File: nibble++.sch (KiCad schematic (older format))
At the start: 19 parts, among them SW1 SW_DPDT_x2, U1 NE555, U2 4017

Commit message: Renamed project to nibble++
Signed-off-by: Thomas Schmid <tom@binary-kitchen.de>
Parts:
- D1: footprint SMD-Challange:LED_0805_2012Metric_Pad1.15x1.40mm_HandSolder_simple_drawing -> nibble++:LED_0805_2012Metric_Pad1.15x1.40mm_HandSolder_simple_drawing
- D2: footprint SMD-Challange:LED_0603_1608Metric_Pad1.05x0.95mm_HandSolder_simple_drawing -> nibble++:LED_0603_1608Metric_Pad1.05x0.95mm_HandSolder_simple_drawing
- D4, D5: footprint SMD-Challange:LED_0201_0603Metric_hand_soldering -> nibble++:LED_0201_0603Metric_hand_soldering
- R1: footprint Resistor_SMD:R_0805_2012Metric_Pad1.15x1.40mm_HandSolder -> nibble++:R_0805_2012Metric_Pad1.15x1.40mm_HandSolder
- R2: footprint Resistor_SMD:R_0603_1608Metric_Pad1.05x0.95mm_HandSolder -> nibble++:R_0603_1608Metric_Pad1.05x0.95mm_HandSolder
- R4: footprint SMD-Challange:R_0201_0603Metric_hand_soldering -> nibble++:R_0201_0603Metric_hand_soldering
- R5: footprint SMD-Challange:R_01005_0402Metric_hand_soldering -> nibble++:R_01005_0402Metric_hand_soldering
- SW1: footprint SMD-Challange:smd_switch_slide -> nibble++:smd_switch_slide
- U2: footprint SMD-Challange:SOP-16_4.4x10.4mm_P1.27mm_simple_drawing -> nibble++:SOP-16_4.4x10.4mm_P1.27mm_simple_drawing
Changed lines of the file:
@@
 EESchema Schematic File Version 4
-LIBS:SMD-Challange-cache
+LIBS:nibble++-cache
 EELAYER 26 0
 EELAYER END
@@
 F 0 "D1" H 7500 2150 50  0000 C CNN
 F 1 "LED" H 7500 2350 50  0000 C CNN
-F 2 "SMD-Challange:LED_0805_2012Metric_Pad1.15x1.40mm_HandSolder_simple_drawing" H 7500 2250 50  0001 C CNN
+F 2 "nibble++:LED_0805_2012Metric_Pad1.15x1.40mm_HandSolder_simple_drawing" H 7500 2250 50  0001 C CNN
 F 3 "~" H 7500 2250 50  0001 C CNN
 	1    7500 2250
@@
 F 0 "D2" H 7500 2450 50  0000 C CNN
 F 1 "LED" H 7500 2650 50  0000 C CNN
-F 2 "SMD-Challange:LED_0603_1608Metric_Pad1.05x0.95mm_HandSolder_simple_drawing" H 7500 2550 50  0001 C CNN
+F 2 "nibble++:LED_0603_1608Metric_Pad1.05x0.95mm_HandSolder_simple_drawing" H 7500 2550 50  0001 C CNN
 F 3 "~" H 7500 2550 50  0001 C CNN
 	1    7500 2550
@@
 F 0 "D4" H 7500 3050 50  0000 C CNN
 F 1 "LED" H 7500 3250 50  0000 C CNN
-F 2 "SMD-Challange:LED_0201_0603Metric_hand_soldering" H 7500 3150 50  0001 C CNN
+F 2 "nibble++:LED_0201_0603Metric_hand_soldering" H 7500 3150 50  0001 C CNN
 F 3 "~" H 7500 3150 50  0001 C CNN
 	1    7500 3150
@@
 F 0 "D5" H 7500 3350 50  0000 C CNN
 F 1 "LED" H 7500 3550 50  0000 C CNN
-F 2 "SMD-Challange:LED_0201_0603Metric_hand_soldering" H 7500 3450 50  0001 C CNN
+F 2 "nibble++:LED_0201_0603Metric_hand_soldering" H 7500 3450 50  0001 C CNN
 F 3 "~" H 7500 3450 50  0001 C CNN
 	1    7500 3450
@@
 F 0 "R1" V 6993 2250 50  0000 C CNN
 F 1 "100" V 7084 2250 50  0000 C CNN
-F 2 "Resistor_SMD:R_0805_2012Metric_Pad1.15x1.40mm_HandSolder" V 7130 2250 50  0001 C CNN
+F 2 "nibble++:R_0805_2012Metric_Pad1.15x1.40mm_HandSolder" V 7130 2250 50  0001 C CNN
 F 3 "~" H 7200 2250 50  0001 C CNN
 	1    7200 2250
@@
 F 0 "R2" V 6993 2550 50  0000 C CNN
 F 1 "100" V 7084 2550 50  0000 C CNN
-F 2 "Resistor_SMD:R_0603_1608Metric_Pad1.05x0.95mm_HandSolder" V 7130 2550 50  0001 C CNN
+F 2 "nibble++:R_0603_1608Metric_Pad1.05x0.95mm_HandSolder" V 7130 2550 50  0001 C CNN
 F 3 "~" H 7200 2550 50  0001 C CNN
 	1    7200 2550
@@
 F 0 "R4" V 6993 3150 50  0000 C CNN
 F 1 "150" V 7084 3150 50  0000 C CNN
-F 2 "SMD-Challange:R_0201_0603Metric_hand_soldering" V 7130 3150 50  0001 C CNN
+F 2 "nibble++:R_0201_0603Metric_hand_soldering" V 7130 3150 50  0001 C CNN
 F 3 "~" H 7200 3150 50  0001 C CNN
 	1    7200 3150
@@
 F 0 "R5" V 6993 3450 50  0000 C CNN
 F 1 "200" V 7084 3450 50  0000 C CNN
-F 2 "SMD-Challange:R_01005_0402Metric_hand_soldering" V 7130 3450 50  0001 C CNN
+F 2 "nibble++:R_01005_0402Metric_hand_soldering" V 7130 3450 50  0001 C CNN
 F 3 "~" H 7200 3450 50  0001 C CNN
 	1    7200 3450
@@
 F 0 "U2" H 5600 3500 50  0000 C CNN
 F 1 "4017" H 5650 3400 50  0000 C CNN
-F 2 "SMD-Challange:SOP-16_4.4x10.4mm_P1.27mm_simple_drawing" H 5850 2750 50  0001 C CNN
+F 2 "nibble++:SOP-16_4.4x10.4mm_P1.27mm_simple_drawing" H 5850 2750 50  0001 C CNN
 F 3 "http://www.intersil.com/content/dam/Intersil/documents/cd40/cd4017bms-22bms.pdf" H 5850 2750 50  0001 C CNN
 	1    5850 2750
@@
 F 0 "SW1" V 3404 1248 50  0000 L CNN
 F 1 "SW_DPDT_x2" V 3495 1248 50  0000 L CNN
-F 2 "SMD-Challange:smd_switch_slide" H 3450 1100 50  0001 C CNN
+F 2 "nibble++:smd_switch_slide" H 3450 1100 50  0001 C CNN
 F 3 "" H 3450 1100 50  0001 C CNN
 	1    3450 1100

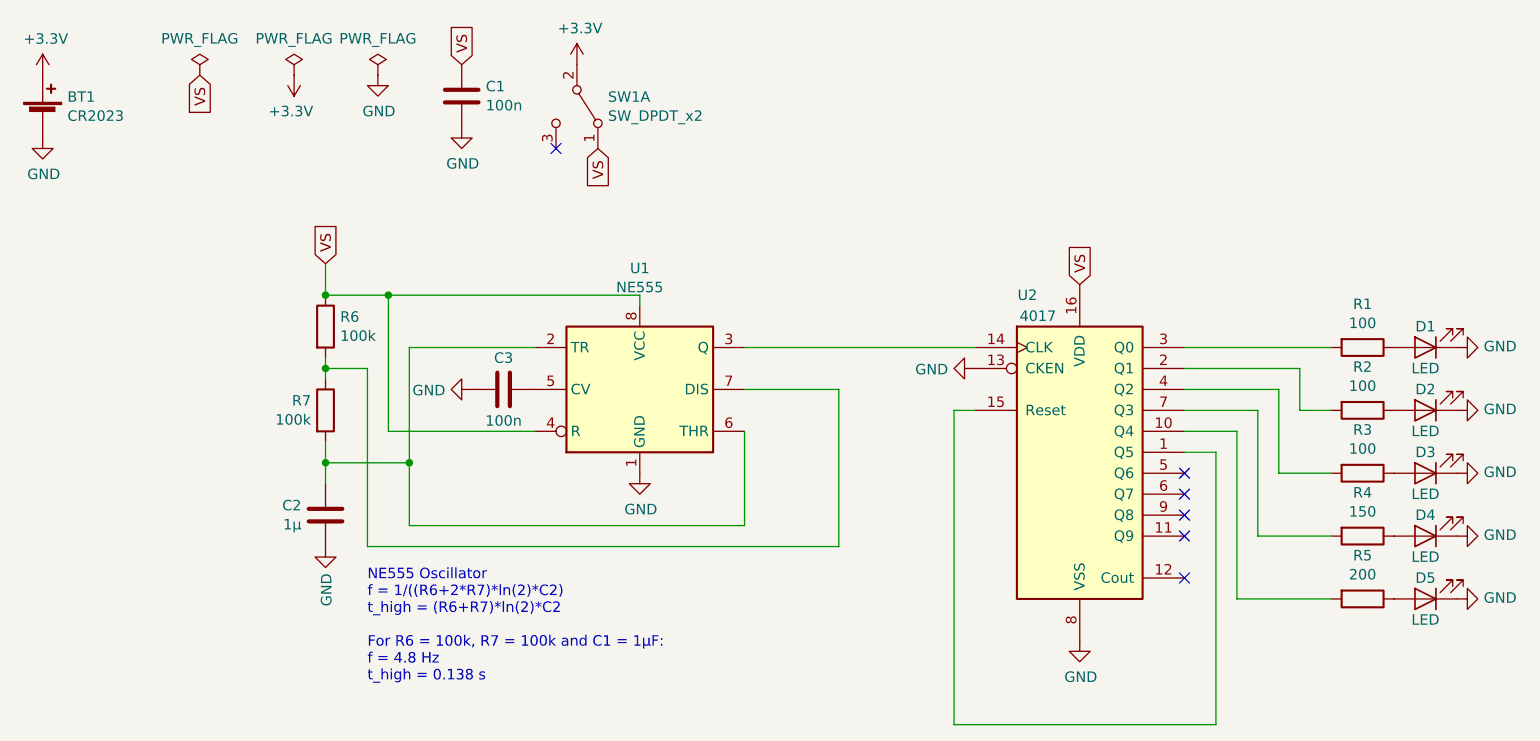
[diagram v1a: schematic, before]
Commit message: added additional information for some parts
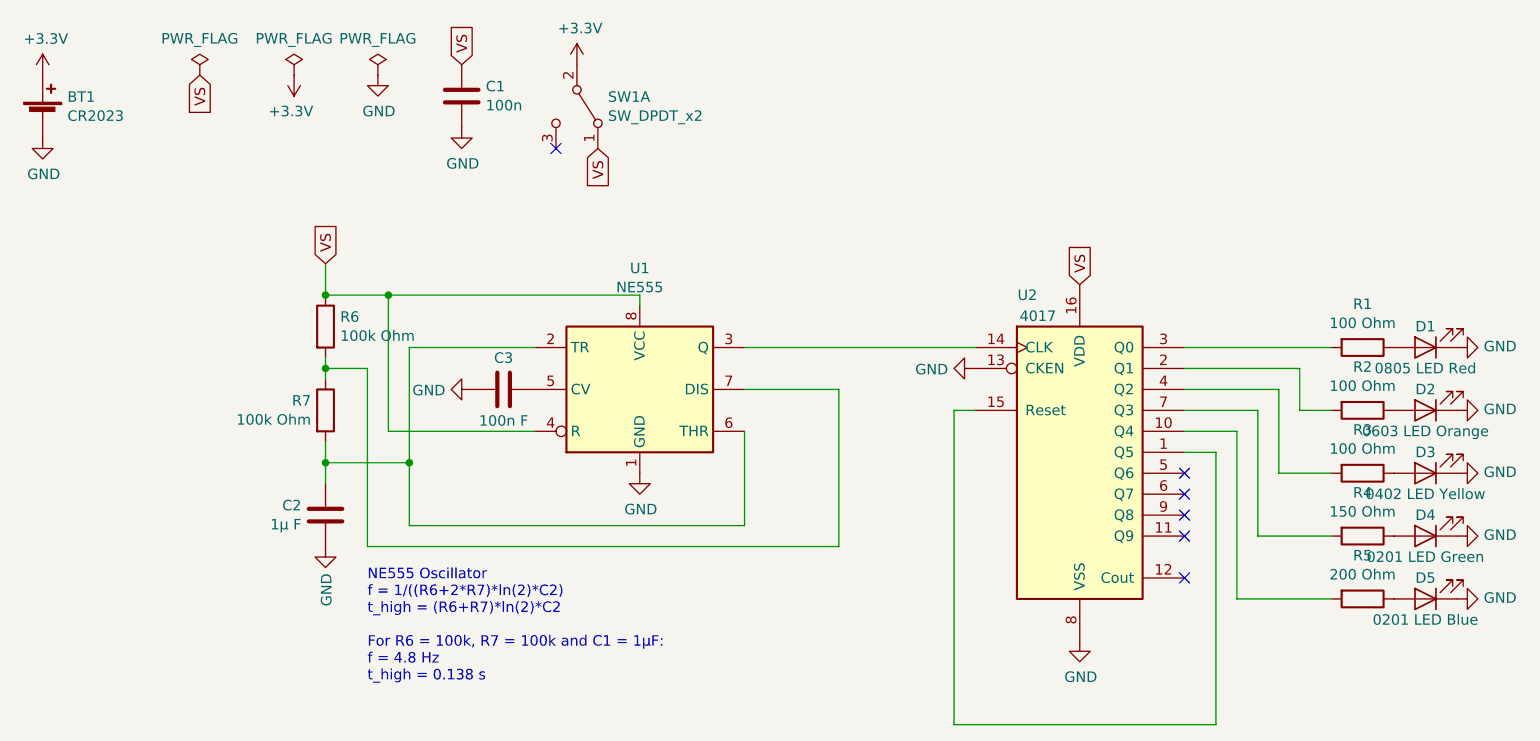
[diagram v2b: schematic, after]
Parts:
- C2: value 1µ -> 1µ F
- C3: value 100n -> 100n F
- D1: value LED -> 0805 LED Red
- D2: value LED -> 0603 LED Orange
- D3: value LED -> 0402 LED Yellow
- D4: value LED -> 0201 LED Green
- D5: value LED -> 0201 LED Blue
- R1, R2, R3: value 100 -> 100 Ohm
- R4: value 150 -> 150 Ohm
- R5: value 200 -> 200 Ohm
- R6, R7: value 100k -> 100k Ohm
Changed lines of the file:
@@
 P 7500 2250
 F 0 "D1" H 7500 2150 50  0000 C CNN
-F 1 "LED" H 7500 2350 50  0000 C CNN
+F 1 "0805 LED Red" H 7500 2350 50  0000 C CNN
 F 2 "nibble++:LED_0805_2012Metric_Pad1.15x1.40mm_HandSolder_simple_drawing" H 7500 2250 50  0001 C CNN
 F 3 "~" H 7500 2250 50  0001 C CNN
@@
 P 7500 2550
 F 0 "D2" H 7500 2450 50  0000 C CNN
-F 1 "LED" H 7500 2650 50  0000 C CNN
+F 1 "0603 LED Orange" H 7500 2650 50  0000 C CNN
 F 2 "nibble++:LED_0603_1608Metric_Pad1.05x0.95mm_HandSolder_simple_drawing" H 7500 2550 50  0001 C CNN
 F 3 "~" H 7500 2550 50  0001 C CNN
@@
 P 7500 2850
 F 0 "D3" H 7500 2750 50  0000 C CNN
-F 1 "LED" H 7500 2950 50  0000 C CNN
+F 1 "0402 LED Yellow" H 7500 2950 50  0000 C CNN
 F 2 "LED_SMD:LED_0402_1005Metric" H 7500 2850 50  0001 C CNN
 F 3 "~" H 7500 2850 50  0001 C CNN
@@
 P 7500 3150
 F 0 "D4" H 7500 3050 50  0000 C CNN
-F 1 "LED" H 7500 3250 50  0000 C CNN
+F 1 "0201 LED Green" H 7500 3250 50  0000 C CNN
 F 2 "nibble++:LED_0201_0603Metric_hand_soldering" H 7500 3150 50  0001 C CNN
 F 3 "~" H 7500 3150 50  0001 C CNN
@@
 P 7500 3450
 F 0 "D5" H 7500 3350 50  0000 C CNN
-F 1 "LED" H 7500 3550 50  0000 C CNN
+F 1 "0201 LED Blue" H 7500 3550 50  0000 C CNN
 F 2 "nibble++:LED_0201_0603Metric_hand_soldering" H 7500 3450 50  0001 C CNN
 F 3 "~" H 7500 3450 50  0001 C CNN
@@
 P 7200 2250
 F 0 "R1" V 6993 2250 50  0000 C CNN
-F 1 "100" V 7084 2250 50  0000 C CNN
+F 1 "100 Ohm" V 7084 2250 50  0000 C CNN
 F 2 "nibble++:R_0805_2012Metric_Pad1.15x1.40mm_HandSolder" V 7130 2250 50  0001 C CNN
 F 3 "~" H 7200 2250 50  0001 C CNN
@@
 P 7200 2550
 F 0 "R2" V 6993 2550 50  0000 C CNN
-F 1 "100" V 7084 2550 50  0000 C CNN
+F 1 "100 Ohm" V 7084 2550 50  0000 C CNN
 F 2 "nibble++:R_0603_1608Metric_Pad1.05x0.95mm_HandSolder" V 7130 2550 50  0001 C CNN
 F 3 "~" H 7200 2550 50  0001 C CNN
@@
 P 7200 2850
 F 0 "R3" V 6993 2850 50  0000 C CNN
-F 1 "100" V 7084 2850 50  0000 C CNN
+F 1 "100 Ohm" V 7084 2850 50  0000 C CNN
 F 2 "Resistor_SMD:R_0402_1005Metric" V 7130 2850 50  0001 C CNN
 F 3 "~" H 7200 2850 50  0001 C CNN
@@
 P 7200 3150
 F 0 "R4" V 6993 3150 50  0000 C CNN
-F 1 "150" V 7084 3150 50  0000 C CNN
+F 1 "150 Ohm" V 7084 3150 50  0000 C CNN
 F 2 "nibble++:R_0201_0603Metric_hand_soldering" V 7130 3150 50  0001 C CNN
 F 3 "~" H 7200 3150 50  0001 C CNN
@@
 P 7200 3450
 F 0 "R5" V 6993 3450 50  0000 C CNN
-F 1 "200" V 7084 3450 50  0000 C CNN
+F 1 "200 Ohm" V 7084 3450 50  0000 C CNN
 F 2 "nibble++:R_01005_0402Metric_hand_soldering" V 7130 3450 50  0001 C CNN
 F 3 "~" H 7200 3450 50  0001 C CNN
@@
 P 3100 2450
 F 0 "C3" V 2950 2450 50  0000 C CNN
-F 1 "100n" V 3250 2450 50  0000 C CNN
+F 1 "100n F" V 3250 2450 50  0000 C CNN
 F 2 "Capacitor_SMD:C_0805_2012Metric_Pad1.15x1.40mm_HandSolder" H 3138 2300 50  0001 C CNN
 F 3 "~" H 3100 2450 50  0001 C CNN
@@
 P 2250 2150
 F 0 "R6" H 2320 2196 50  0000 L CNN
-F 1 "100k" H 2320 2105 50  0000 L CNN
+F 1 "100k Ohm" H 2320 2105 50  0000 L CNN
 F 2 "Resistor_SMD:R_0805_2012Metric_Pad1.15x1.40mm_HandSolder" V 2180 2150 50  0001 C CNN
 F 3 "~" H 2250 2150 50  0001 C CNN
@@
 P 2250 2550
 F 0 "R7" H 2181 2596 50  0000 R CNN
-F 1 "100k" H 2181 2505 50  0000 R CNN
+F 1 "100k Ohm" H 2181 2505 50  0000 R CNN
 F 2 "Resistor_SMD:R_0805_2012Metric_Pad1.15x1.40mm_HandSolder" V 2180 2550 50  0001 C CNN
 F 3 "~" H 2250 2550 50  0001 C CNN
@@
 P 2250 3050
 F 0 "C2" H 2365 3004 50  0000 L CNN
-F 1 "1µ" H 2365 3095 50  0000 L CNN
+F 1 "1µ F" H 2365 3095 50  0000 L CNN
 F 2 "Capacitor_SMD:C_0805_2012Metric_Pad1.15x1.40mm_HandSolder" H 2288 2900 50  0001 C CNN
 F 3 "~" H 2250 3050 50  0001 C CNN

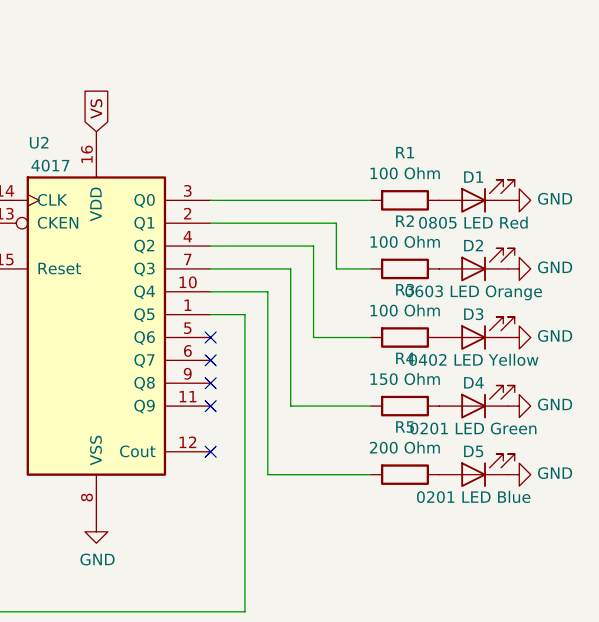
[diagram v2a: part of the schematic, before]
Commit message: modified resistor value. fixing #3
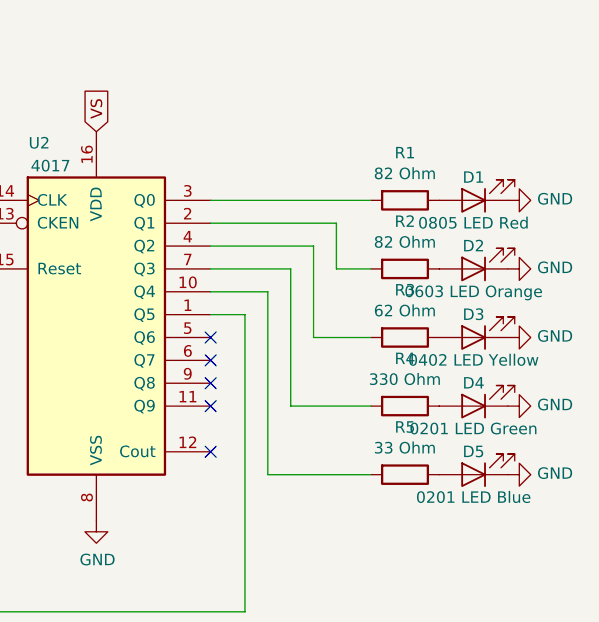
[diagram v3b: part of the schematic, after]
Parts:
- R1, R2: value 100 Ohm -> 82 Ohm
- R3: value 100 Ohm -> 62 Ohm
- R4: value 150 Ohm -> 330 Ohm
- R5: value 200 Ohm -> 33 Ohm
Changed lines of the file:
@@
 EESchema Schematic File Version 4
 LIBS:nibble++-cache
-EELAYER 26 0
+EELAYER 29 0
 EELAYER END
 $Descr A4 11693 8268
@@
 P 7200 2250
 F 0 "R1" V 6993 2250 50  0000 C CNN
-F 1 "100 Ohm" V 7084 2250 50  0000 C CNN
+F 1 "82 Ohm" V 7084 2250 50  0000 C CNN
 F 2 "nibble++:R_0805_2012Metric_Pad1.15x1.40mm_HandSolder" V 7130 2250 50  0001 C CNN
 F 3 "~" H 7200 2250 50  0001 C CNN
@@
 P 7200 2550
 F 0 "R2" V 6993 2550 50  0000 C CNN
-F 1 "100 Ohm" V 7084 2550 50  0000 C CNN
+F 1 "82 Ohm" V 7084 2550 50  0000 C CNN
 F 2 "nibble++:R_0603_1608Metric_Pad1.05x0.95mm_HandSolder" V 7130 2550 50  0001 C CNN
 F 3 "~" H 7200 2550 50  0001 C CNN
@@
 P 7200 2850
 F 0 "R3" V 6993 2850 50  0000 C CNN
-F 1 "100 Ohm" V 7084 2850 50  0000 C CNN
+F 1 "62 Ohm" V 7084 2850 50  0000 C CNN
 F 2 "Resistor_SMD:R_0402_1005Metric" V 7130 2850 50  0001 C CNN
 F 3 "~" H 7200 2850 50  0001 C CNN
@@
 P 7200 3150
 F 0 "R4" V 6993 3150 50  0000 C CNN
-F 1 "150 Ohm" V 7084 3150 50  0000 C CNN
+F 1 "330 Ohm" V 7084 3150 50  0000 C CNN
 F 2 "nibble++:R_0201_0603Metric_hand_soldering" V 7130 3150 50  0001 C CNN
 F 3 "~" H 7200 3150 50  0001 C CNN
@@
 P 7200 3450
 F 0 "R5" V 6993 3450 50  0000 C CNN
-F 1 "200 Ohm" V 7084 3450 50  0000 C CNN
+F 1 "33 Ohm" V 7084 3450 50  0000 C CNN
 F 2 "nibble++:R_01005_0402Metric_hand_soldering" V 7130 3450 50  0001 C CNN
 F 3 "~" H 7200 3450 50  0001 C CNN
